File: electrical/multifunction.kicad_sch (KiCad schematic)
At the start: 15 parts

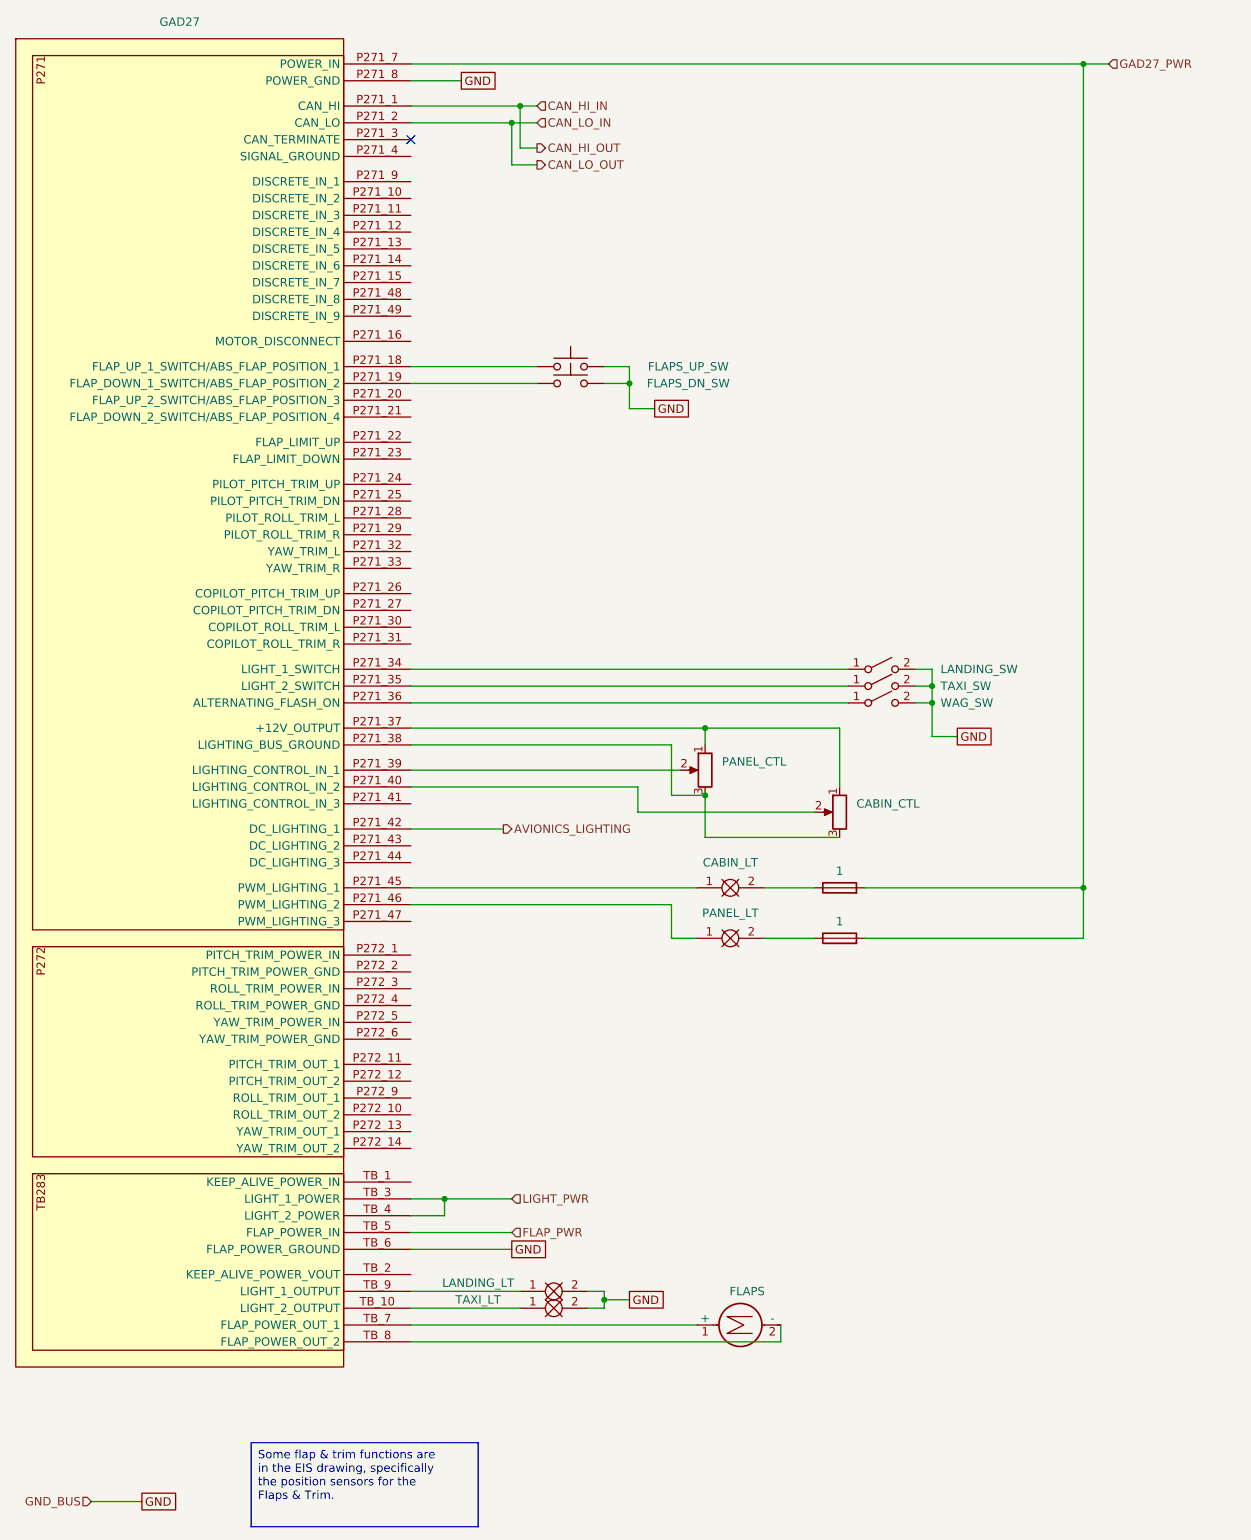
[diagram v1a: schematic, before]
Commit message: Added Warning/Caution lights/buttons. Moved smoke on to GAD 27. Added glide button to GAD 27. Added lighting switched pots to GEA 24.
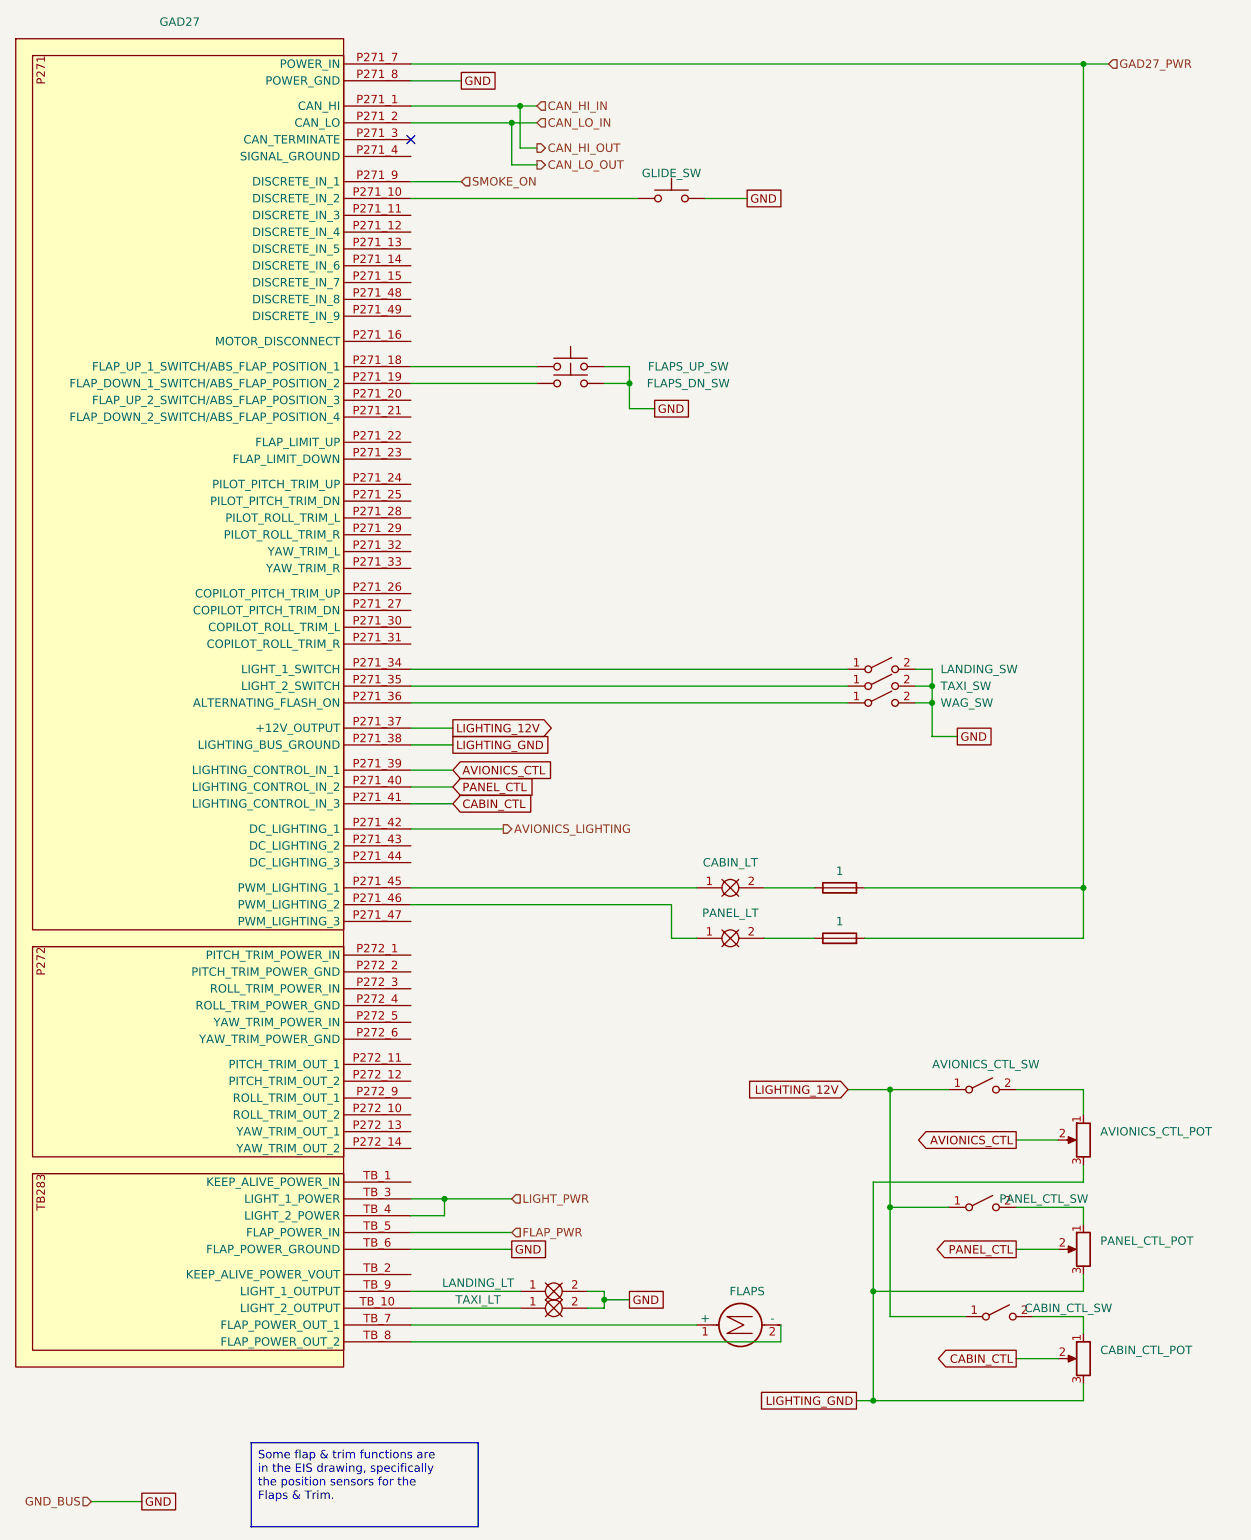
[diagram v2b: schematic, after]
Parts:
- removed CABIN_CTL, PANEL_CTL: LIGHTS_REOSTAT, symbol Device:R_Potentiometer
- added AVIONICS_CTL_POT, CABIN_CTL_POT, PANEL_CTL_POT: LIGHTS_REOSTAT, symbol Device:R_Potentiometer
- added AVIONICS_CTL_SW, CABIN_CTL_SW, PANEL_CTL_SW: ~, symbol Switch:SW_SPST
- added GLIDE_SW: SW_Push, symbol Switch:SW_Push
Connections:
- net GND: now also GLIDE_SW.2
- net at GAD27.P271_10 (DISCRETE_IN_2): now also GLIDE_SW.1
- net LIGHTING_12V: now reaches GAD27.P271_37 (+12V_OUTPUT)
- net LIGHTING_12V: now also AVIONICS_CTL_SW.1 (A), CABIN_CTL_SW.1 (A), PANEL_CTL_SW.1 (A)
- net LIGHTING_GND: now reaches GAD27.P271_38 (LIGHTING_BUS_GROUND)
- net LIGHTING_GND: now also AVIONICS_CTL_POT.3, CABIN_CTL_POT.3, PANEL_CTL_POT.3
- net AVIONICS_CTL: now reaches GAD27.P271_39 (LIGHTING_CONTROL_IN_1)
- net AVIONICS_CTL: now also AVIONICS_CTL_POT.2
- net PANEL_CTL: now reaches GAD27.P271_40 (LIGHTING_CONTROL_IN_2)
- net PANEL_CTL: now also PANEL_CTL_POT.2
- net CABIN_CTL: now reaches GAD27.P271_41 (LIGHTING_CONTROL_IN_3)
- net CABIN_CTL: now also CABIN_CTL_POT.2
- net SMOKE_ON: now reaches GAD27.P271_9 (DISCRETE_IN_1)
- new net: AVIONICS_CTL_POT.1, AVIONICS_CTL_SW.2 (B)
- new net: CABIN_CTL_POT.1, CABIN_CTL_SW.2 (B)
- new net: PANEL_CTL_POT.1, PANEL_CTL_SW.2 (B)

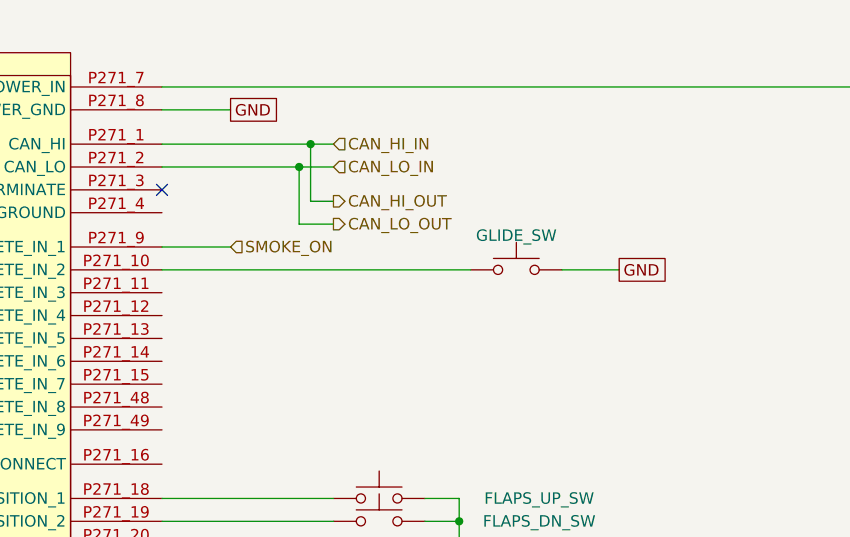
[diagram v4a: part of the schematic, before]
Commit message: Updated electrical to not use IBBS. Also, added BT adapter and 3P3T switch.
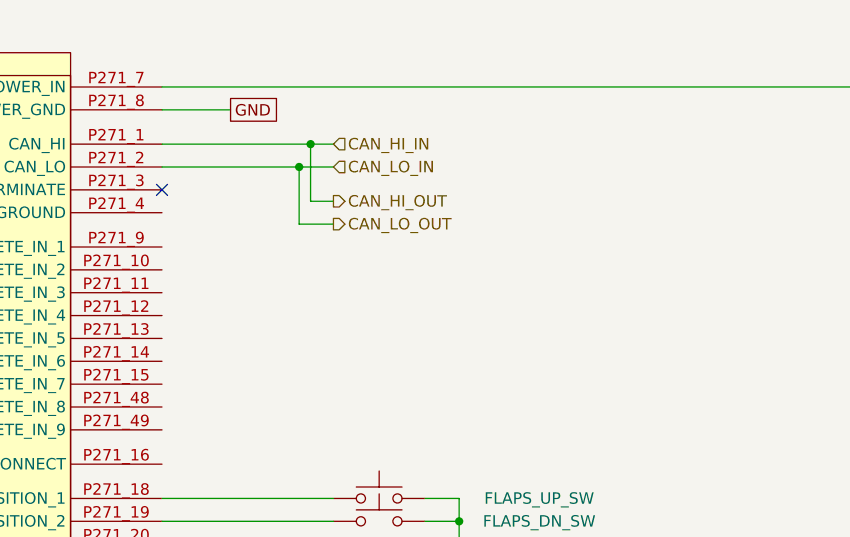
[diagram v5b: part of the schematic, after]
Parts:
- removed GLIDE_SW: SW_Push, symbol Switch:SW_Push
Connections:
- net SMOKE_ON: no longer names the net of GAD27.P271_9 (DISCRETE_IN_1)
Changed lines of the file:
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@@
-    (stroke (width 0) (type default))
-  )
-  (wire (pts (xy 125.73 46.99) (xy 132.08 46.99))
     (stroke (width 0) (type default))
   )
@@
     (stroke (width 0) (type default))
   )
-  (wire (pts (xy 81.28 44.45) (xy 88.9 44.45))
-    (stroke (width 0) (type default))
-  )
   (wire (pts (xy 81.28 212.09) (xy 97.79 212.09))
     (stroke (width 0) (type default))
@@
   )
   (wire (pts (xy 114.3 74.93) (xy 114.3 72.39))
-    (stroke (width 0) (type default))
-  )
-  (wire (pts (xy 81.28 46.99) (xy 115.57 46.99))
     (stroke (width 0) (type default))
   )
@@
     )
   )
-  (global_label "GND" (shape passive) (at 132.08 46.99 0) (fields_autoplaced)
-    (effects (font (size 1.27 1.27)) (justify left))
-    (property "Intersheetrefs" "${INTERSHEET_REFS}" (at 137.8244 46.99 0)
-      (effects (font (size 1.27 1.27)) (justify left) hide)
-    )
-  )
   (global_label "LIGHTING_12V" (shape output) (at 87.63 127 0) (fields_autoplaced)
     (effects (font (size 1.27 1.27)) (justify left))
@@
   )
   (hierarchical_label "LIGHT_PWR" (shape input) (at 96.52 198.12 0) (fields_autoplaced)
-    (effects (font (size 1.27 1.27)) (justify left))
-  )
-  (hierarchical_label "SMOKE_ON" (shape input) (at 88.9 44.45 0) (fields_autoplaced)
     (effects (font (size 1.27 1.27)) (justify left))
   )
@@
         )
       )
-    )
-  )
-  (symbol (lib_id "Switch:SW_Push") (at 120.65 46.99 0) (unit 1)
-    (in_bom yes) (on_board yes) (dnp no)
-    (property "Reference" "GLIDE_SW" (at 120.65 43.18 0)
-      (effects (font (size 1.27 1.27)))
-    )
-    (property "Value" "SW_Push" (at 120.65 41.91 0)
-      (effects (font (size 1.27 1.27)) hide)
-    )
-    (property "Footprint" "" (at 120.65 41.91 0)
-      (effects (font (size 1.27 1.27)) hide)
-    )
-    (property "Datasheet" "~" (at 120.65 41.91 0)
-      (effects (font (size 1.27 1.27)) hide)
-    )
-    (pin "1")
-    (pin "2")
-    (instances
-      (project "electrical"
-        (path "/e8ec215a-dbe2-4eba-a577-e50a0a128049/67540fe5-9b6d-4d8c-9d03-cde1487f48ae"
-          (reference "GLIDE_SW") (unit 1)
-        )
-      )

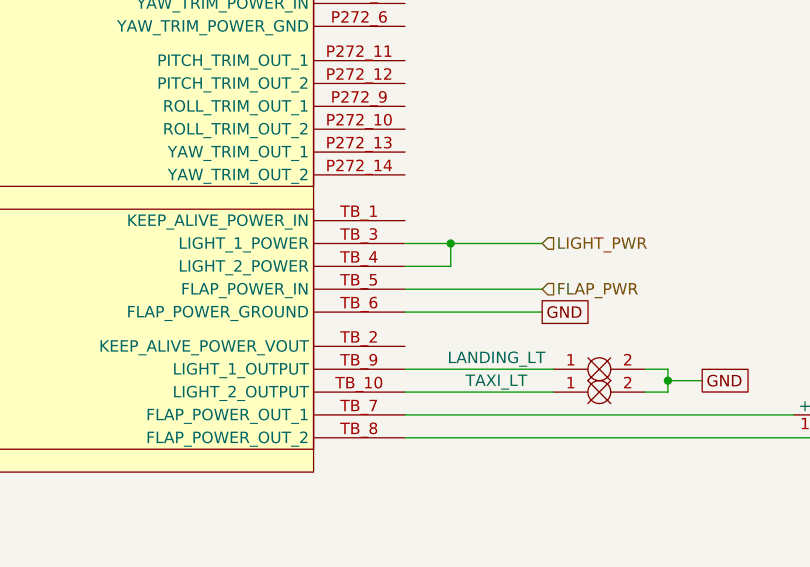
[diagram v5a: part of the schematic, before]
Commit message: Changed to have ELT with GPS. Also, changed Flaps to have position sensor. Added in wiring for all the sensors.
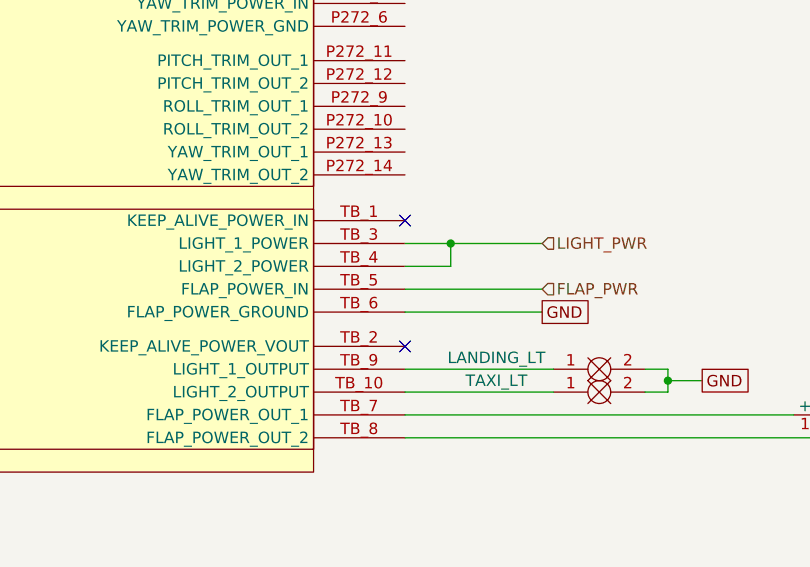
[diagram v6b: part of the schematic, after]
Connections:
- no-connect marks 1 -> 3
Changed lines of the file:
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@@
   (junction (at 151.13 228.6) (diameter 0) (color 0 0 0 0)
   )
+  (no_connect (at 81.28 209.55))
   (no_connect (at 81.28 38.1))
+  (no_connect (at 81.28 195.58))
   (wire (pts (xy 81.28 74.93) (xy 100.33 74.93))
     (stroke (width 0) (type default))
